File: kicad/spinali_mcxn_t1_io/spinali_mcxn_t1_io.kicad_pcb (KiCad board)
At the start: 4 copper layers, 36.5 x 46 mm, 76 parts, among them J1 DF40TC(4.0)-50DS-0.4V(51), J10 SPI2, J11 ESC1, J12 ESC2, J13 RTC_BAT, J2 DF40TC(4.0)-50DS-0.4V(51), J3 I2C1, J4 I2C2, J5 UART1, J6 UART2, J7 QDEC, J8 GPS, J9 SPI1, Q1 NX138BKMYL, SW1 CHS-01TA

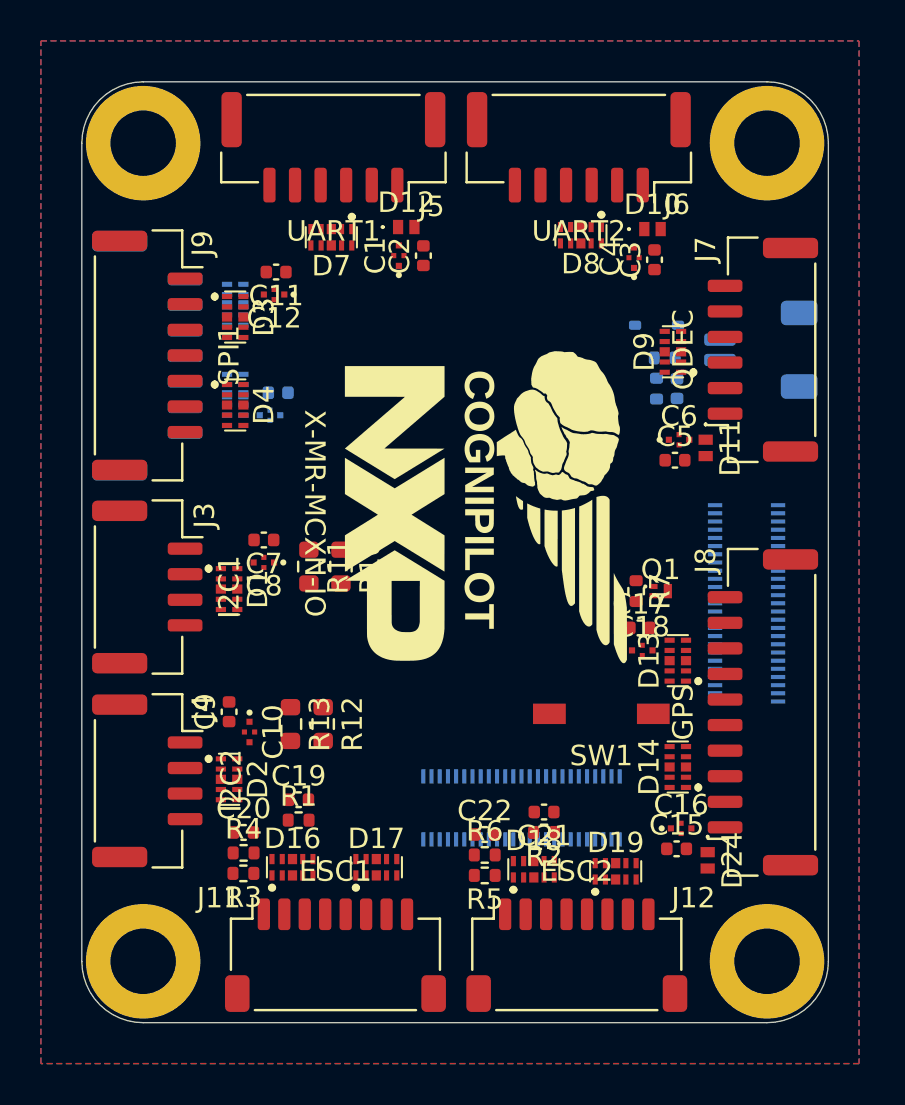
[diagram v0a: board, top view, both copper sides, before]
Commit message: Finished IO board layout positioning. Started routing.
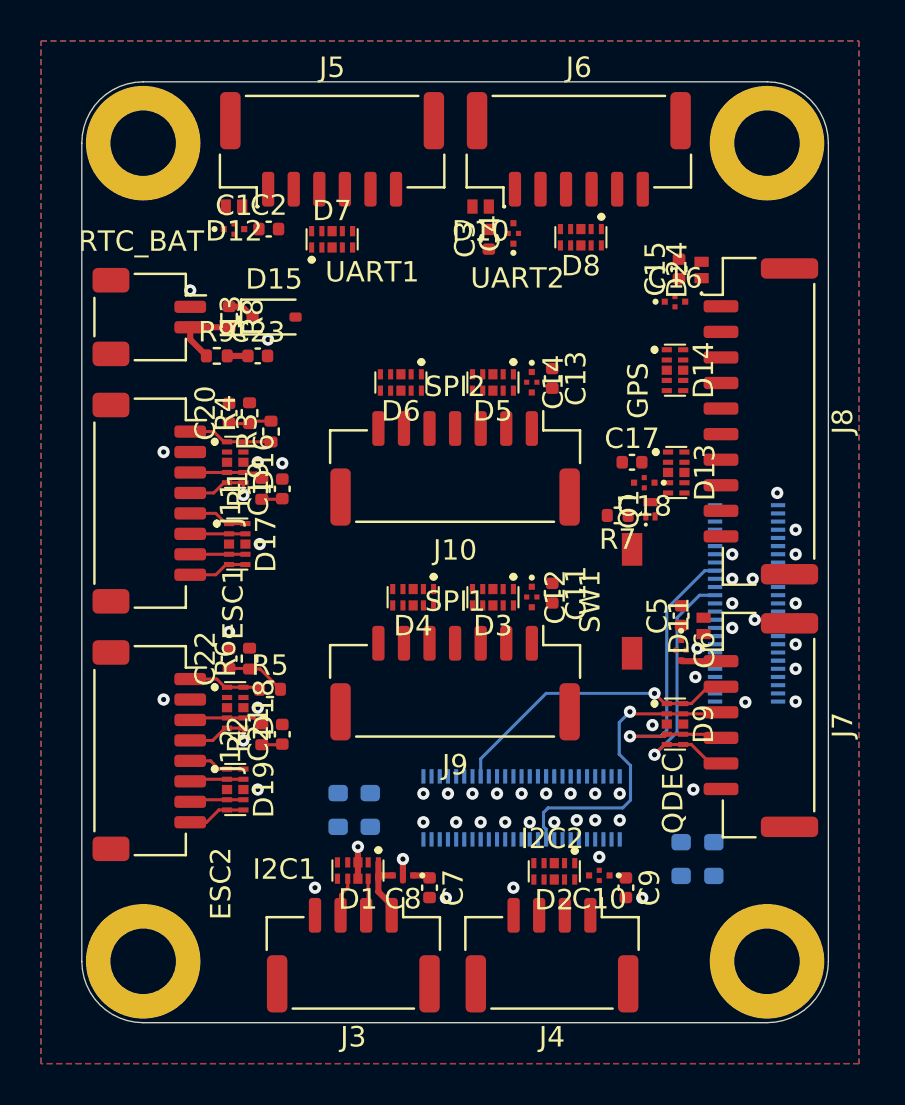
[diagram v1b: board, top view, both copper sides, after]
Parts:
- C13, C14, C23, D15, D5, D6, J13, R8, R9: moved to F.Cu
- G***, R10, R11, R12, R13: moved to B.Cu
- J10: footprint Connector_JST:JST_GH_SM07B-GHS-TB_1x07-1MP_P1.25mm_Horizontal -> Connector_JST:JST_GH_BM07B-GHS-TBT_1x07-1MP_P1.25mm_Vertical; moved to F.Cu
- J3, J4: footprint Connector_JST:JST_GH_SM04B-GHS-TB_1x04-1MP_P1.25mm_Horizontal -> Connector_JST:JST_GH_BM04B-GHS-TBT_1x04-1MP_P1.25mm_Vertical
- J5, J6, J7: footprint Connector_JST:JST_GH_SM06B-GHS-TB_1x06-1MP_P1.25mm_Horizontal -> Connector_JST:JST_GH_BM06B-GHS-TBT_1x06-1MP_P1.25mm_Vertical
- J8: footprint Connector_JST:JST_GH_SM10B-GHS-TB_1x10-1MP_P1.25mm_Horizontal -> Connector_JST:JST_GH_BM10B-GHS-TBT_1x10-1MP_P1.25mm_Vertical
- J9: footprint Connector_JST:JST_GH_SM07B-GHS-TB_1x07-1MP_P1.25mm_Horizontal -> Connector_JST:JST_GH_BM07B-GHS-TBT_1x07-1MP_P1.25mm_Vertical
- moved J13 29.9 mm to (120.3, 63.5)
- moved D24 28.9 mm to (147.3, 61.2), turned to 90 degrees
- moved C15 28.4 mm to (146.2, 61.1), turned to 90 degrees
- moved C16 25.8 mm to (146.0, 62.8)
- moved J11 23.9 mm to (120.3, 72.6), turned to -90 degrees
- moved J12 23.2 mm to (120.3, 84.7), turned to -90 degrees
- moved J9 22.0 mm to (135.2, 81.4), turned to 180 degrees
- moved R3 21.6 mm to (126.2, 69.1), turned to 90 degrees
- moved R9 21.6 mm to (123.6, 65.4), turned to 0 degrees
- moved J4 21.5 mm to (140.0, 94.7), turned to 180 degrees
- moved R4 21.5 mm to (125.2, 68.2), turned to 90 degrees
- moved R8 21.4 mm to (124.2, 63.5), turned to -90 degrees
- moved C9 21.2 mm to (143.6, 91.4), turned to -90 degrees
- moved C11 20.7 mm to (140.0, 77.0), turned to -90 degrees
- moved J3 20.6 mm to (130.3, 94.7), turned to 180 degrees
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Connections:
- D16 pad 9: unconnected-(D16-IO_2-Pad2)_1 -> unconnected-(D16-IO_2-Pad2)
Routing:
- net P2_6/TRIG_IN4_QDEC2_PA: track 0.00 -> 15.6 mm, vias 0 -> 1
- net P1_22/TRIG_IN3_QDEC1_PB: track 0.00 -> 15.2 mm, vias 0 -> 1
- net P4_20/TRIG_IN8_QDEC1_PA: track 0.00 -> 14.5 mm, vias 0 -> 1
- net P2_0/TRIG_IN5_QDEC2_PB: track 0.00 -> 13.3 mm, vias 0 -> 1
- net P2_3/FC9_P1_UART_TXD: track 0.00 -> 6.86 mm, vias 0 -> 2
- net /IO2/VBAT1: track 0.00 -> 4.16 mm
- net /IO1/I2C1_5V: track 0.00 -> 3.72 mm
- net /IO2/CURR2: track 0.00 -> 3.66 mm
- net Net-(J13-1-Pad2): track 0.00 -> 3.63 mm
- net /IO2/CURR1: track 0.00 -> 3.62 mm
- net /IO2/VBAT2: track 0.00 -> 3.60 mm
- net P1_16/ADC1_A16: track 0.00 -> 2.93 mm
- net P3_11/PWM0_B3: track 0.00 -> 2.91 mm
- net P3_0/PWM0_A0: track 0.00 -> 2.91 mm
- net P2_1/PWM1_B3: track 0.00 -> 2.85 mm
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
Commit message: Initial routing of IO board done.
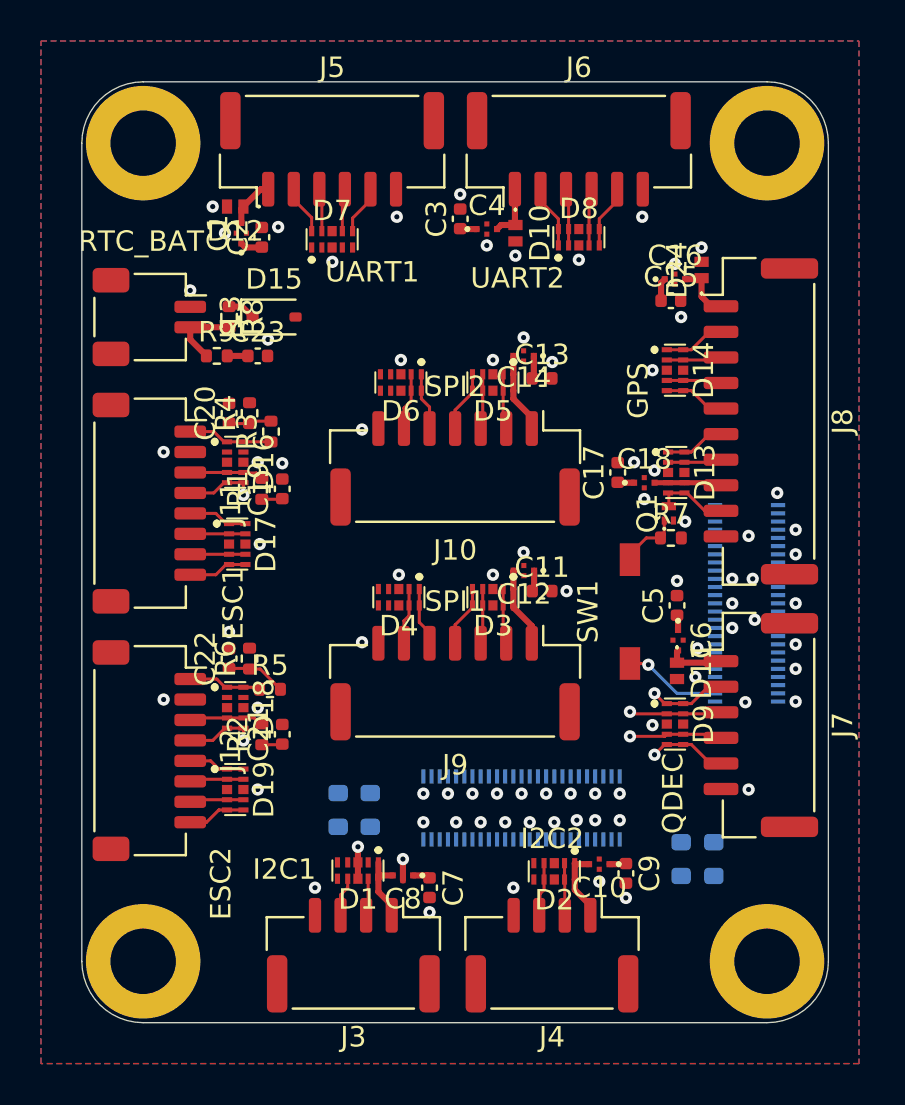
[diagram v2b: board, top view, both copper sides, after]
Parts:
- moved R7 2.82 mm to (145.8, 74.3), turned to 0 degrees
- moved D11 2.56 mm to (146.1, 80.8), turned to -90 degrees
- moved D10 2.14 mm to (138.2, 59.4), turned to -90 degrees
- moved C3 1.72 mm to (135.5, 58.7)
- moved C15 1.60 mm to (145.8, 62.7), turned to 0 degrees
- moved C14 1.35 mm to (138.6, 65.4), turned to 180 degrees
- moved C12 1.34 mm to (138.6, 75.9), turned to 180 degrees
- moved C4 1.32 mm to (136.8, 59.2), turned to 0 degrees
- moved C16 1.10 mm to (146.0, 61.6)
- moved Q1 0.92 mm to (145.7, 73.1)
- moved C17 0.86 mm to (143.2, 71.1), turned to 90 degrees
- moved C9 0.70 mm to (143.6, 90.7)
- moved D4 0.70 mm to (132.5, 77.2)
- moved C10 0.55 mm to (142.3, 90.2)
- moved C5 0.54 mm to (146.1, 77.6)
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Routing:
- net P2_6/TRIG_IN4_QDEC2_PA: track 15.6 -> 4.56 mm
- net P4_20/TRIG_IN8_QDEC1_PA: track 14.5 -> 3.80 mm
- net P1_22/TRIG_IN3_QDEC1_PB: track 15.2 -> 4.58 mm
- net P2_0/TRIG_IN5_QDEC2_PB: track 13.3 -> 3.84 mm
- net +5V: track 0.85 -> 7.60 mm
- net P1_0/FC3_P0_I2C_SDA: track 0.00 -> 5.66 mm
- net P1_1/FC3_P1_I2C_SCL: track 0.00 -> 5.26 mm
- net P3_12/CT1_MAT2_BUZZER: track 0.00 -> 4.78 mm, vias 0 -> 1
- net /IO1/SPI1_5V: track 0.00 -> 3.93 mm
- net /IO1/SPI2_5V: track 0.00 -> 3.92 mm
- net /IO2/GPS_BUZZER: track 0.00 -> 3.62 mm
- net /IO1/I2C2_5V: track 0.00 -> 3.59 mm
- net /IO2/GPS_3V3: track 0.00 -> 3.30 mm
- net P0_18/FC0_P2_UART_RTS: track 0.00 -> 3.11 mm
- net P0_17/FC0_P1_UART_TXD: track 0.00 -> 3.11 mm
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
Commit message: Finished Routing IO board
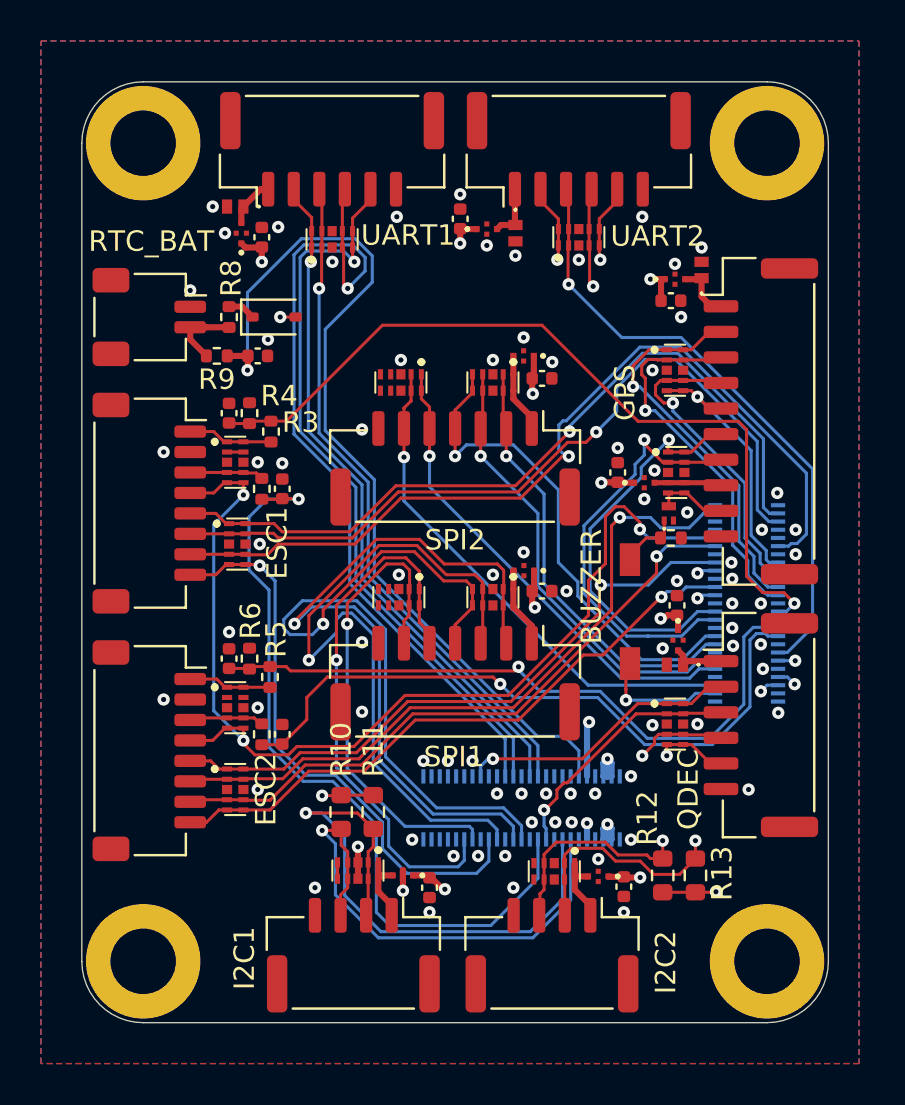
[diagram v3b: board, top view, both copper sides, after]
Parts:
- R10, R11, R12, R13: moved to F.Cu
- moved G*** 4.42 mm to (135.4, 73.4), turned to 180 degrees
- moved R12 2.62 mm to (145.4, 90.8)
- moved R13 1.06 mm to (147.0, 90.8)
- moved C9 0.66 mm to (143.5, 91.3)
- moved C10 0.60 mm to (142.2, 90.8)
- moved R5 0.60 mm to (126.2, 81.1), turned to 90 degrees
- moved D11 0.32 mm to (146.0, 80.5), turned to 180 degrees
- moved R10 0.18 mm to (129.7, 87.7)
- moved R11 0.18 mm to (131.2, 87.7)
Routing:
- net +3V3: track 0.81 -> 71.2 mm, vias 0 -> 6
- net P2_3/FC9_P1_UART_TXD: track 6.86 -> 51.7 mm, vias 2 -> 3
- net VDD_BAT: track 1.01 -> 45.4 mm, vias 0 -> 1
- net P1_1/FC3_P1_I2C_SCL: track 5.26 -> 49.5 mm, vias 0 -> 2
- net P1_0/FC3_P0_I2C_SDA: track 5.66 -> 49.0 mm, vias 0 -> 2
- net P3_9/PWM0_B2: track 2.70 -> 43.2 mm, vias 0 -> 1
- net P4_3/FC2_P3_UART_CTS: track 2.10 -> 40.6 mm, vias 0 -> 1
- net P1_18/ADC1_A18: track 2.11 -> 40.5 mm, vias 0 -> 1
- net P1_23/ADC1_A23: track 1.01 -> 38.4 mm, vias 0 -> 1
- net P3_7/PWM0_B1: track 2.70 -> 38.4 mm, vias 0 -> 1
- net P3_0/PWM0_A0: track 2.91 -> 38.1 mm, vias 0 -> 1
- net P4_2/FC2_P2_UART_RTS: track 2.41 -> 36.6 mm, vias 0 -> 1
- net P3_1/FC6_P0_SPI_SDO: track 3.00 -> 36.6 mm, vias 0 -> 1
- net P3_6/FC6_P1_SPI_SCK: track 2.71 -> 36.1 mm, vias 0 -> 1
- net P3_10/FC6_P2_SPI_SDI: track 2.69 -> 34.9 mm, vias 0 -> 1
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- added copper zone on In2.Cu, net +5V
- added copper zone on In3.Cu, net GND
- added copper zone on In4.Cu, net GND
- removed copper zone on In2.Cu, net GND
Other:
- copper layers 4 -> 6
- board text added: "BUZZER"

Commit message: Updated IO board layout to 4-layers
- Re-routed a bit so 4-layers is possible.
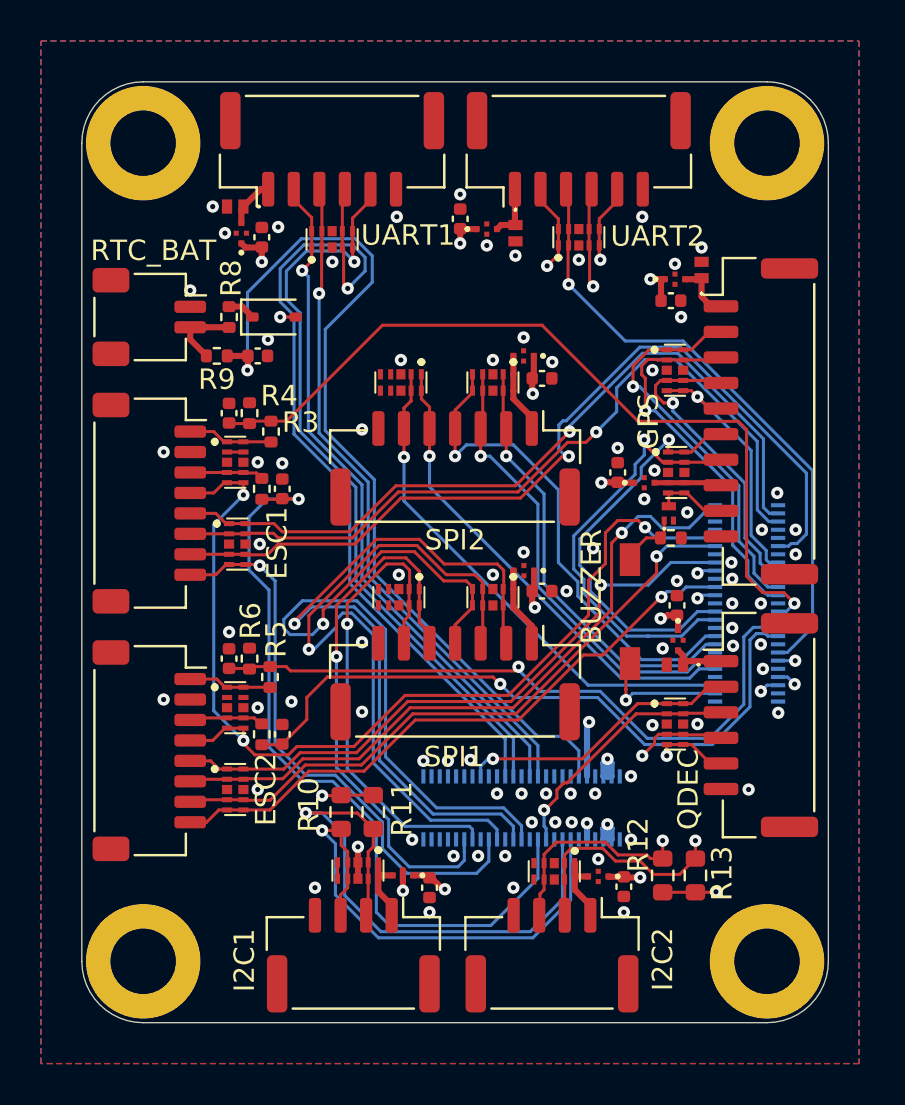
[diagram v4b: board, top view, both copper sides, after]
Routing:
- net P2_3/FC9_P1_UART_TXD: track 51.7 -> 50.5 mm
- net P3_10/FC6_P2_SPI_SDI: track 34.9 -> 34.0 mm
- net P0_17/FC0_P1_UART_TXD: track 30.4 -> 31.2 mm
- net P4_3/FC2_P3_UART_CTS: track 40.6 -> 41.2 mm
- net P4_2/FC2_P2_UART_RTS: track 36.6 -> 37.2 mm
- net GND: vias 81 -> 83
- removed copper zone on In3.Cu, net GND
- removed copper zone on In4.Cu, net GND
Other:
- copper layers 6 -> 4

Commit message: Created production files for IO board
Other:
- board text added: "1"
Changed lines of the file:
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@@
 		(layer "Edge.Cuts")
+	)
+	(gr_text "1"
+		(at 126.85 59.1 0)
+		(layer "F.SilkS")
+		(effects
+			(font
+				(size 1 1)
+				(thickness 0.15)
+			)
+		)
+	)
+	(gr_text "1"
+		(at 123 79.95 90)
+		(layer "F.SilkS")
+		(effects
+			(font
+				(size 1 1)
+				(thickness 0.15)
+			)
+		)
 	)
 	(gr_text "BUZZER"
@@
 		)
 	)
+	(gr_text "1"
+		(at 123 61.65 90)
+		(layer "F.SilkS")
+		(effects
+			(font
+				(size 1 1)
+				(thickness 0.15)
+			)
+		)
+	)
+	(gr_text "1"
+		(at 123 67.8 90)
+		(layer "F.SilkS")
+		(effects
+			(font
+				(size 1 1)
+				(thickness 0.15)
+			)
+		)
+	)
+	(gr_text "1"
+		(at 133.35 92.05 0)
+		(layer "F.SilkS")
+		(effects
+			(font
+				(size 1 1)
+				(thickness 0.15)
+			)
+		)
+	)
+	(gr_text "1"
+		(at 146.3 63.75 90)
+		(layer "F.SilkS")
+		(effects
+			(font
+				(size 1 1)
+				(thickness 0.15)
+			)
+		)
+	)
+	(gr_text "1"
+		(at 142.9 91.925 0)
+		(layer "F.SilkS")
+		(effects
+			(font
+				(size 1 1)
+				(thickness 0.15)
+			)
+		)
+	)
+	(gr_text "1"
+		(at 136.9 58.1 0)
+		(layer "F.SilkS")
+		(effects
+			(font
+				(size 1 1)
+				(thickness 0.15)
+			)
+		)
+	)
+	(gr_text "1"
+		(at 147.5 79.1 90)
+		(layer "F.SilkS")
+		(effects
+			(font
+				(size 1 1)
+				(thickness 0.15)
+			)
+		)
+	)
